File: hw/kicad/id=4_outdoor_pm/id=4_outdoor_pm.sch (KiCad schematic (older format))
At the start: 58 parts, among them IC1 LPS22HB, IC2 24AA02T-I_OT, IC3 SHT30-DIS-B, IC4 SN74AUP1T17DCKR, IC5 nRF52840-QIAA-T, J1 53047-0810, Q1 NMOS_DGS, Q2 NMOS_DGS, Y1 32MHZ, Y2 32.768K

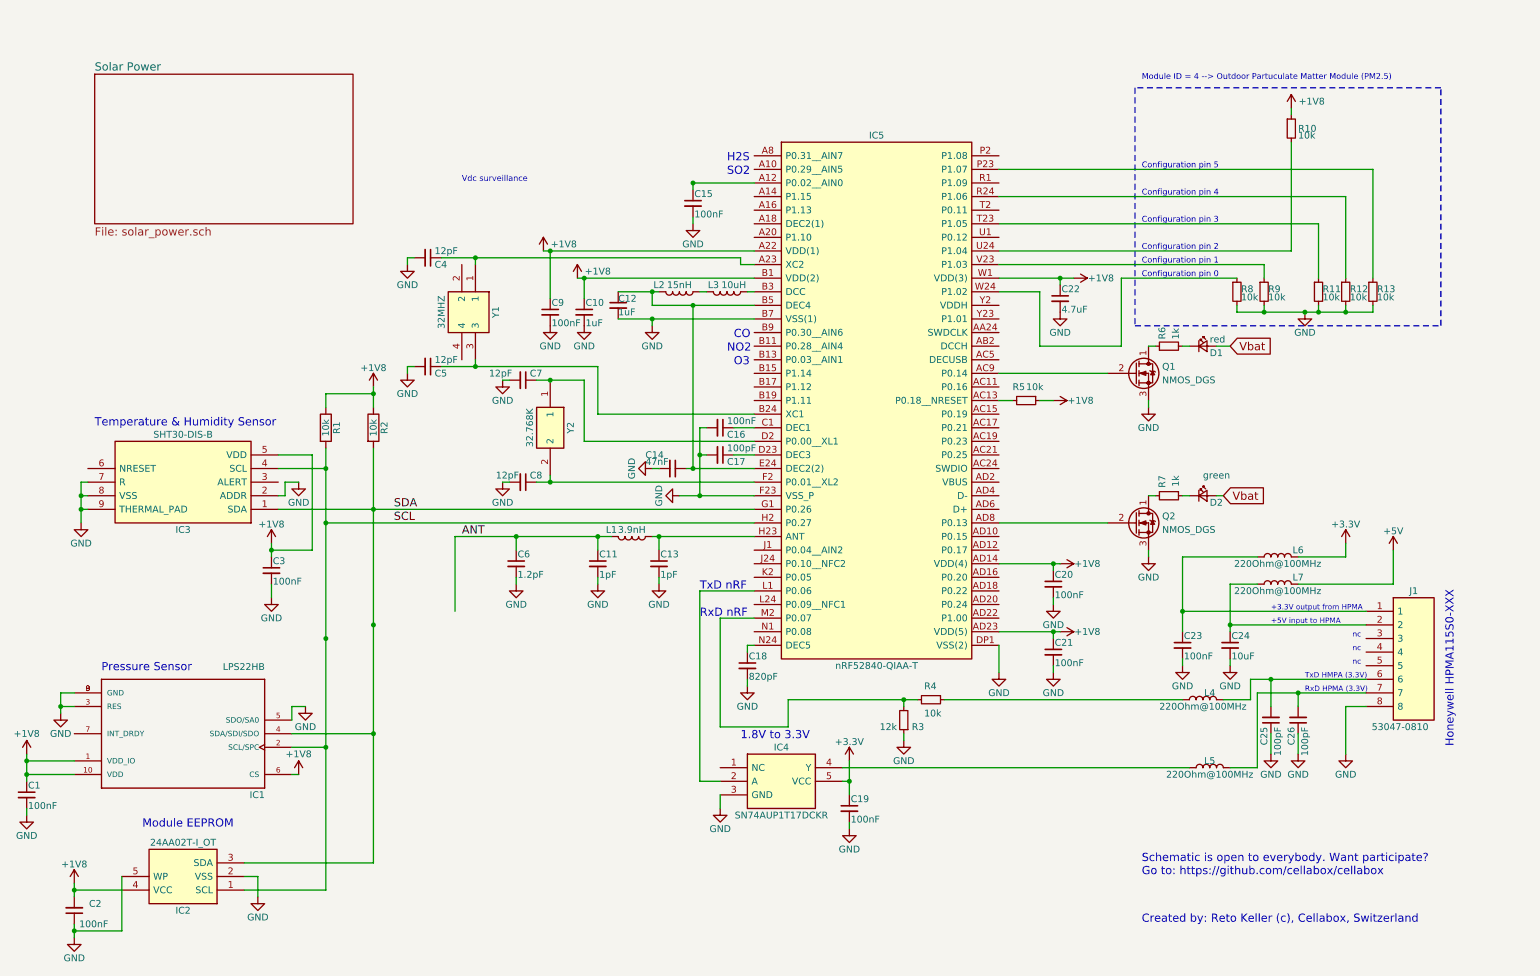
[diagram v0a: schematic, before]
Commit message: Datasheets added Schematic for outdoor PM extended
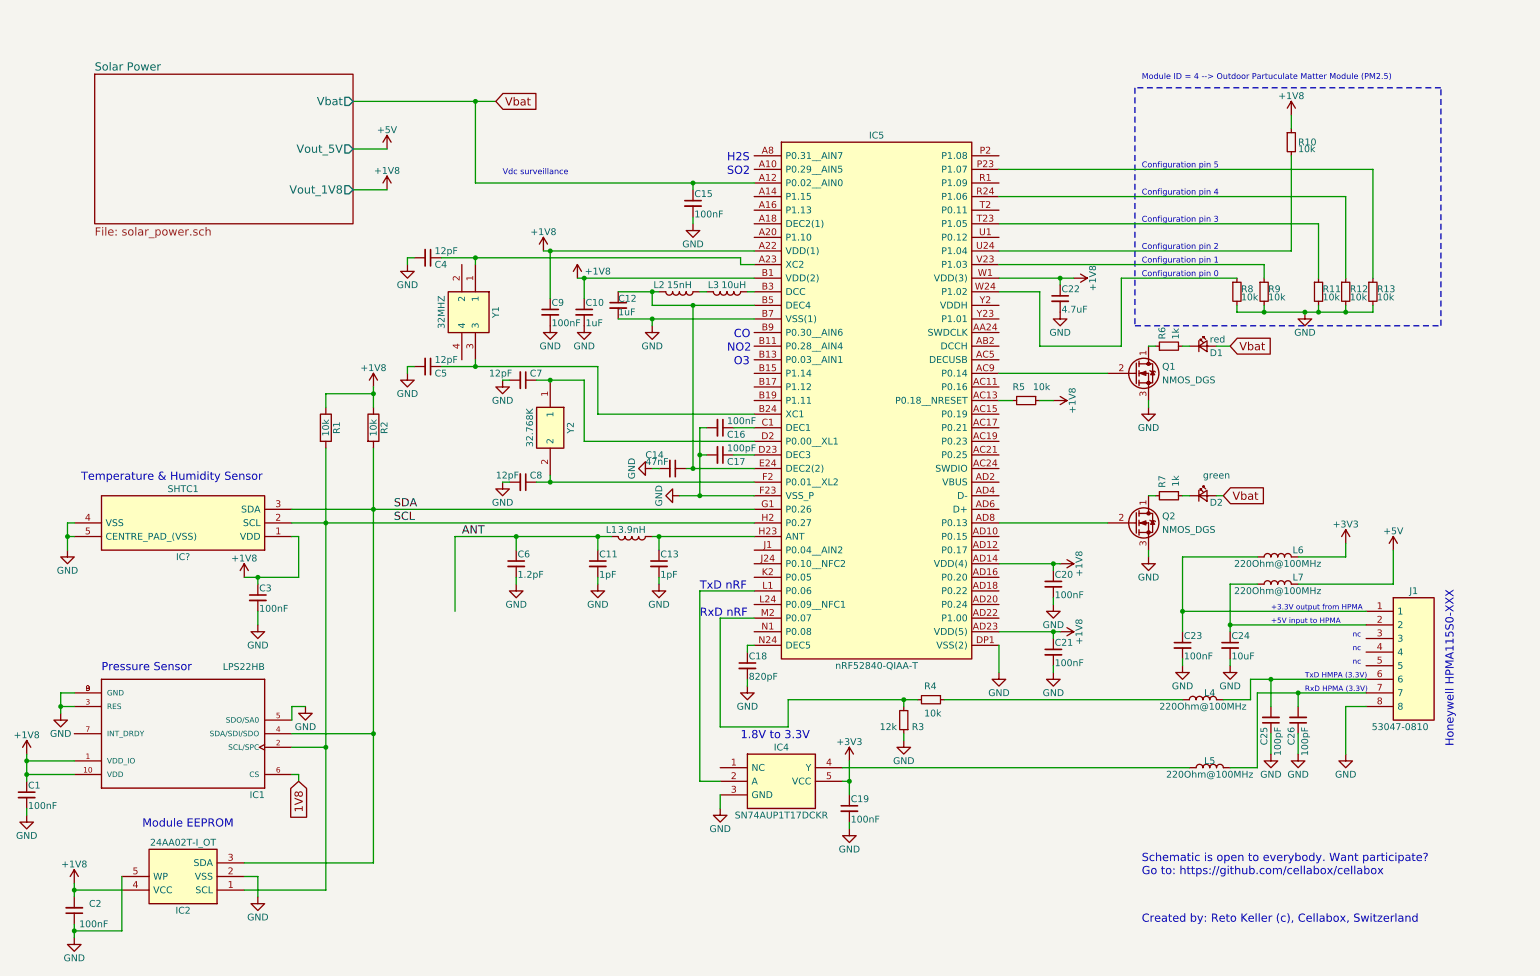
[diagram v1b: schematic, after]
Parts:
- removed IC3: SHT30-DIS-B, SON50P250X250X100-9N, symbol SHT30-DIS-B
- added IC?: SHTC1, SON100P200X200X7500-5N, symbol SHTC1
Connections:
- net +1V8: now also IC?.1 (VDD); no longer IC1.6 (CS)
- net GND: now also IC?.4 (VSS), IC?.5 (CENTRE_PAD_(VSS))
- net SCL: now also IC?.2 (SCL)
- net SDA: now also IC?.3 (SDA)
- net Vbat: now also C15.1, IC5.A12 (P0.02__AIN0)
- new net 1V8: IC1.6 (CS)
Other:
- moved on the sheet: C3, R10

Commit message: Updated schematics: battery surveillance.
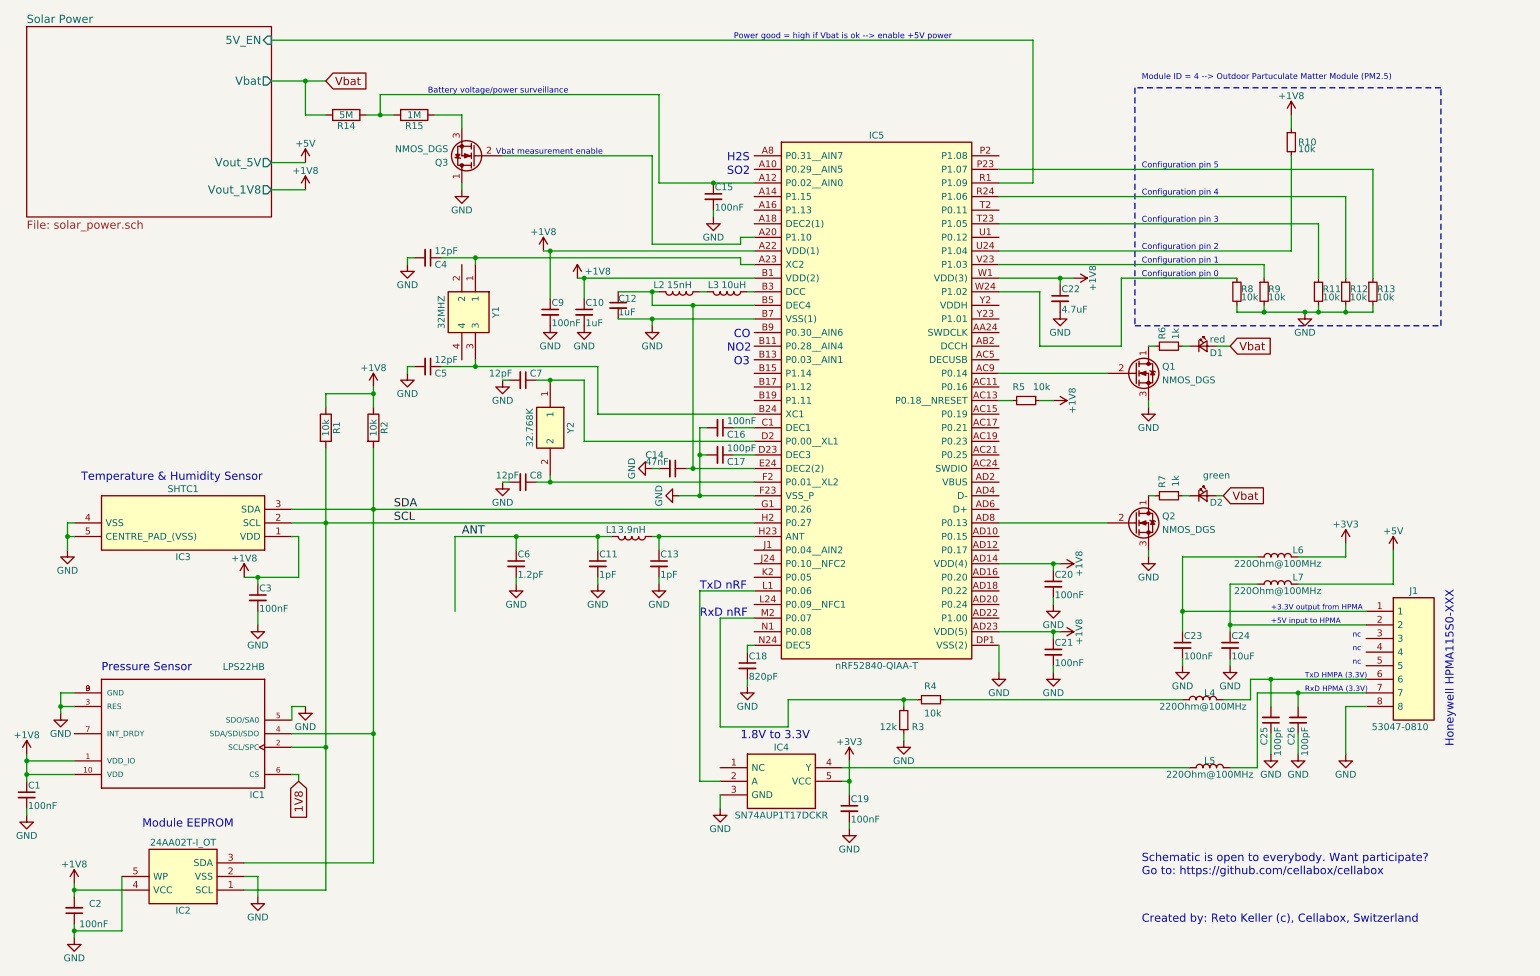
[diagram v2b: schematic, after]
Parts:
- added Q3: NMOS_DGS, symbol Q_NMOS_DGS
- added R14: 5M, symbol R
- added R15: 1M, symbol R
- gave numbers to parts that had none: 1
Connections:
- net GND: now also Q3.1 (D)
- net Vbat: now also R14.2; no longer C15.1, IC5.A12 (P0.02__AIN0)
- net at IC5.A20 (P1.10): now also Q3.2 (G)
- net Solar Power/5V_EN: now reaches IC5.R1 (P1.09)
- new net: C15.1, IC5.A12 (P0.02__AIN0), R14.1, R15.2
- new net: Q3.3 (S), R15.1
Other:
- note added: "Battery voltage/power surveillance"
- note added: "Power good = high if Vbat is ok --> enable +5V power"
- note added: "Vbat measurement enable"
- note removed: "Vdc surveillance"
- moved on the sheet: C15
